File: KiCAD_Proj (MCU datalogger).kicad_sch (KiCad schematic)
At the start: 25 parts, among them U1 24LC1025-I_SM, U2 DS1337S_, U3 24LC1025-I_SM, U4 ATMEGA328P-AU, Y1 32.768 KHz, Y2 16MHz

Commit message: Fixed bugs in schematic.
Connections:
- net SCK: no longer R3.2, U1.6 (SCL), U2.6 (SCL), U3.6 (SCL), U4.28 (PC5)
- new net SCL: R3.2, U1.6 (SCL), U2.6 (SCL), U3.6 (SCL), U4.28 (PC5)
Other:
- sheet Untitled Sheet ports: added SCL; removed SCK
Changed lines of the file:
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@@
 	)
 	(junction
-		(at 245.11 44.45)
-		(diameter 0)
-		(color 0 0 0 0)
-	)
-	(junction
 		(at 232.41 95.25)
 		(diameter 0)
@@
 	(wire
 		(pts
-			(xy 245.11 36.83) (xy 245.11 44.45)
-		)
-		(stroke
-			(width 0)
-			(type default)
-		)
-	)
-	(wire
-		(pts
 			(xy 139.7 62.23) (xy 139.7 74.93)
 		)
@@
 	(wire
 		(pts
-			(xy 245.11 44.45) (xy 251.46 44.45)
+			(xy 241.3 44.45) (xy 251.46 44.45)
 		)
 		(stroke
@@
 	(wire
 		(pts
-			(xy 241.3 44.45) (xy 245.11 44.45)
-		)
-		(stroke
-			(width 0)
-			(type default)
-		)
-	)
-	(wire
-		(pts
 			(xy 241.3 95.25) (xy 246.38 95.25)
 		)
@@
 		)
 	)
-	(label "SCK"
+	(label "SCL"
 		(at 161.29 133.35 180)
 		(effects
@@
 		)
 	)
-	(label "SCK"
+	(label "SCL"
 		(at 104.14 140.97 0)
 		(effects
@@
 		)
 	)
-	(label "SCK"
+	(label "SCL"
 		(at 49.53 48.26 180)
 		(effects
@@
 		)
 	)
-	(label "SCK"
+	(label "SCL"
 		(at 55.88 140.97 0)
 		(effects
@@
 		)
 	)
-	(label "SCK"
+	(label "SCL"
 		(at 195.58 87.63 180)
 		(effects
@@
 		)
 	)
-	(label "SCK"
+	(label "SCL"
 		(at 116.84 151.13 0)
 		(effects
@@
 	)
 	(symbol
-		(lib_id "power:PWR_FLAG")
-		(at 245.11 36.83 0)
-		(unit 1)
-		(exclude_from_sim no)
-		(in_bom yes)
-		(on_board yes)
-		(dnp no)
-		(fields_autoplaced yes)
-		(property "Reference" "#FLG02"
-			(at 245.11 34.925 0)
-			(effects
-				(font
-					(size 1.27 1.27)
-				)
-				(hide yes)
-			)
-		)
-		(property "Value" "PWR_FLAG"
-			(at 245.11 31.75 0)
-			(effects
-				(font
-					(size 1.27 1.27)
-				)
-			)
-		)
-		(property "Footprint" ""
-			(at 245.11 36.83 0)
-			(effects
-				(font
-					(size 1.27 1.27)
-				)
-				(hide yes)
-			)
-		)
-		(property "Datasheet" "~"
-			(at 245.11 36.83 0)
-			(effects
-				(font
-					(size 1.27 1.27)
-				)
-				(hide yes)
-			)
-		)
-		(property "Description" "Special symbol for telling ERC where power comes from"
-			(at 245.11 36.83 0)
-			(effects
-				(font
-					(size 1.27 1.27)
-				)
-				(hide yes)
-			)
-		)
-		(property "Purpose" ""
-			(at 245.11 36.83 0)
-			(effects
-				(font
-					(size 1.27 1.27)
-				)
-			)
-		)
-		(pin "1"
-		)
-		(instances
-			(project ""
-				(path "/4bd39814-648a-43e5-9d59-9775154104be"
-					(reference "#FLG02")
-					(unit 1)
-				)
-			)
-		)
-	)
-	(symbol
 		(lib_id "power:GND")
 		(at 109.22 71.12 0)
@@
 			)
 		)
-		(pin "SCK" passive
+		(pin "SCL" passive
 			(at 161.29 133.35 180)
 			(effects

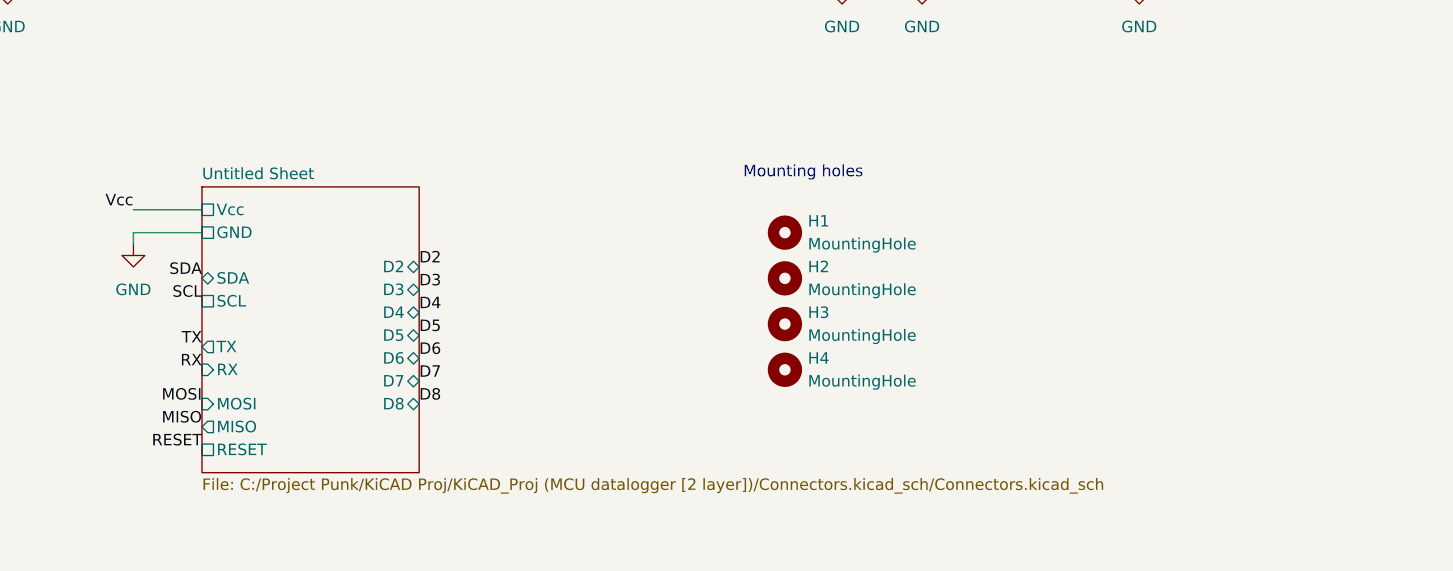
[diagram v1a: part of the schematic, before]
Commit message: Fixing the bug on PCB.
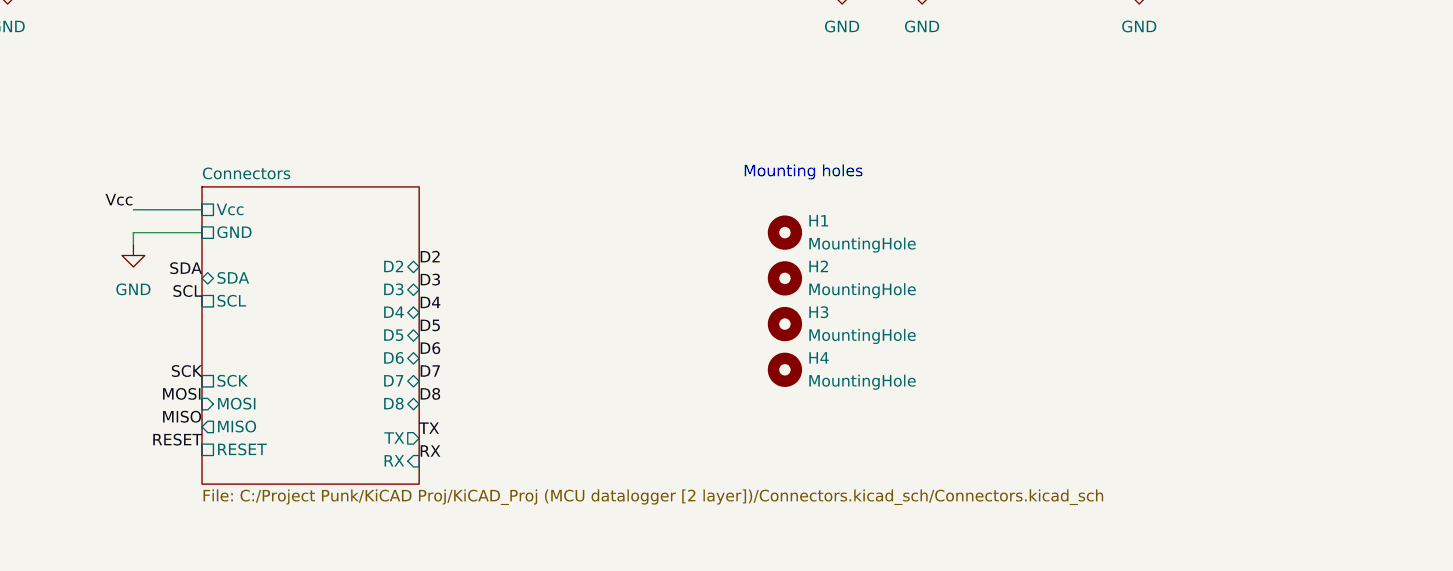
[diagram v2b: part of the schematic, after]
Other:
- sheet Untitled Sheet renamed Connectors
- sheet Connectors ports: added SCK; removed none
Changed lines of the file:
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@@
 		)
 	)
-	(label "RX"
-		(at 161.29 140.97 180)
-		(effects
-			(font
-				(size 1.27 1.27)
-			)
-			(justify right bottom)
-		)
-	)
 	(label "D4"
 		(at 185.42 134.62 0)
@@
 		)
 	)
+	(label "TX"
+		(at 185.42 148.59 0)
+		(effects
+			(font
+				(size 1.27 1.27)
+			)
+			(justify left bottom)
+		)
+	)
 	(label "SCL"
 		(at 116.84 151.13 0)
@@
 		)
 	)
-	(label "Vcc"
-		(at 30.48 143.51 180)
+	(label "RX"
+		(at 185.42 151.13 0)
 		(effects
 			(font
 				(size 1.27 1.27)
 			)
-			(justify right bottom)
+			(justify left bottom)
 		)
 	)
-	(label "TX"
-		(at 161.29 138.43 180)
+	(label "Vcc"
+		(at 30.48 143.51 180)
 		(effects
 			(font
@@
 		)
 	)
+	(label "SCK"
+		(at 161.29 142.24 180)
+		(effects
+			(font
+				(size 1.27 1.27)
+			)
+			(justify right bottom)
+		)
+	)
 	(label "D3"
 		(at 185.42 132.08 0)
@@
 	(sheet
 		(at 161.29 120.65)
-		(size 24.13 31.75)
+		(size 24.13 33.02)
 		(exclude_from_sim no)
 		(in_bom yes)
@@
 			(color 0 0 0 0.0000)
 		)
-		(property "Sheetname" "Untitled Sheet"
+		(property "Sheetname" "Connectors"
 			(at 161.29 119.9384 0)
 			(effects
@@
 		)
 		(property "Sheetfile" "C:/Project Punk/KiCAD Proj/KiCAD_Proj (MCU datalogger [2 layer])/Connectors.kicad_sch/Connectors.kicad_sch"
-			(at 161.29 152.9846 0)
+			(at 161.29 154.2546 0)
 			(effects
 				(font
@@
 		)
 		(pin "RX" input
-			(at 161.29 140.97 180)
+			(at 185.42 151.13 0)
 			(effects
 				(font
 					(size 1.27 1.27)
 				)
-				(justify left)
+				(justify right)
 			)
 		)
@@
 		)
 		(pin "TX" output
-			(at 161.29 138.43 180)
+			(at 185.42 148.59 0)
+			(effects
+				(font
+					(size 1.27 1.27)
+				)
+				(justify right)
+			)
+		)
+		(pin "SCK" passive
+			(at 161.29 142.24 180)
 			(effects
 				(font

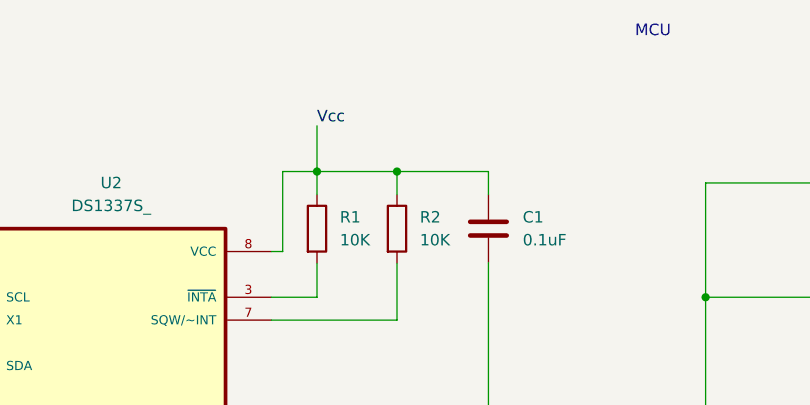
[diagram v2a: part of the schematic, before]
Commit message: Fixed the rule areas.
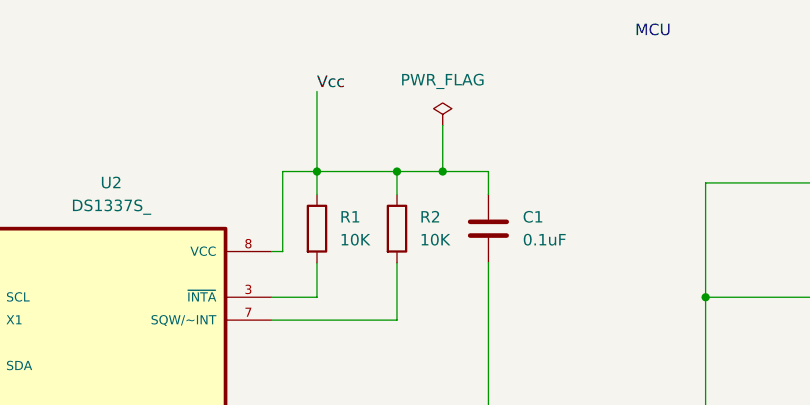
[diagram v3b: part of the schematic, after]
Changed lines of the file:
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@@
 	)
 	(junction
+		(at 104.14 34.29)
+		(diameter 0)
+		(color 0 0 0 0)
+	)
+	(junction
 		(at 232.41 95.25)
 		(diameter 0)
@@
 	(wire
 		(pts
-			(xy 90.17 29.21) (xy 90.17 34.29)
+			(xy 90.17 25.4) (xy 90.17 34.29)
 		)
 		(stroke
@@
 	(wire
 		(pts
-			(xy 99.06 34.29) (xy 109.22 34.29)
+			(xy 99.06 34.29) (xy 104.14 34.29)
 		)
 		(stroke
@@
 	(wire
 		(pts
+			(xy 104.14 34.29) (xy 109.22 34.29)
+		)
+		(stroke
+			(width 0)
+			(type default)
+		)
+	)
+	(wire
+		(pts
 			(xy 129.54 135.89) (xy 129.54 133.35)
 		)
@@
 	(wire
 		(pts
+			(xy 104.14 29.21) (xy 104.14 34.29)
+		)
+		(stroke
+			(width 0)
+			(type default)
+		)
+	)
+	(wire
+		(pts
 			(xy 156.21 48.26) (xy 167.64 48.26)
 		)
@@
 	)
 	(label "Vcc"
-		(at 90.17 29.21 0)
+		(at 90.17 25.4 0)
 		(effects
 			(font
@@
 			)
 			(stroke
-				(width 0)
-				(type dash)
+				(width 0.254)
+				(type solid)
+				(color 0 0 139 1)
 			)
 			(fill
@@
 			)
 			(stroke
-				(width 0)
-				(type dash)
+				(width 0.254)
+				(type solid)
+				(color 0 0 139 1)
 			)
 			(fill
@@
 			)
 			(stroke
-				(width 0)
-				(type dash)
+				(width 0.254)
+				(type solid)
+				(color 0 0 139 1)
 			)
 			(fill
@@
 			)
 			(stroke
-				(width 0)
-				(type dash)
+				(width 0.254)
+				(type solid)
+				(color 0 0 139 1)
 			)
 			(fill
@@
 					(unit 1)
 				)
+			)
+		)
+	)
+	(symbol
+		(lib_id "power:PWR_FLAG")
+		(at 104.14 29.21 0)
+		(unit 1)
+		(exclude_from_sim no)
+		(in_bom yes)
+		(on_board yes)
+		(dnp no)
+		(fields_autoplaced yes)
+		(property "Reference" "#FLG02"
+			(at 104.14 27.305 0)
+			(effects
+				(font
+					(size 1.27 1.27)
+				)
+				(hide yes)
+			)
+		)
+		(property "Value" "PWR_FLAG"
+			(at 104.14 24.13 0)
+			(effects
+				(font
+					(size 1.27 1.27)
+				)
+			)
+		)
+		(property "Footprint" ""
+			(at 104.14 29.21 0)
+			(effects
+				(font
+					(size 1.27 1.27)
+				)
+				(hide yes)
+			)
+		)
+		(property "Datasheet" "~"
+			(at 104.14 29.21 0)
+			(effects
+				(font
+					(size 1.27 1.27)
+				)
+				(hide yes)
+			)
+		)
+		(property "Description" "Special symbol for telling ERC where power comes from"
+			(at 104.14 29.21 0)
+			(effects
+				(font
+					(size 1.27 1.27)
+				)
+				(hide yes)
+			)
+		)
+		(pin "1"
+		)
+		(instances
+			(project ""
+				(path "/4bd39814-648a-43e5-9d59-9775154104be"
+					(reference "#FLG02")
+					(unit 1)
+				)
